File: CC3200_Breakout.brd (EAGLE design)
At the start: 69.8 x 88.9 mm, 101 parts, among them J1 MJ-3536N, J3 SJ-3515-SMT, J4 SJ-3515-SMT, U1 TLV320AIC3254_RHB_32, U15 AT25FS010, U2 TPA2012D2_RTJ_20, Y2 32.768KHz, Y3 407MHz

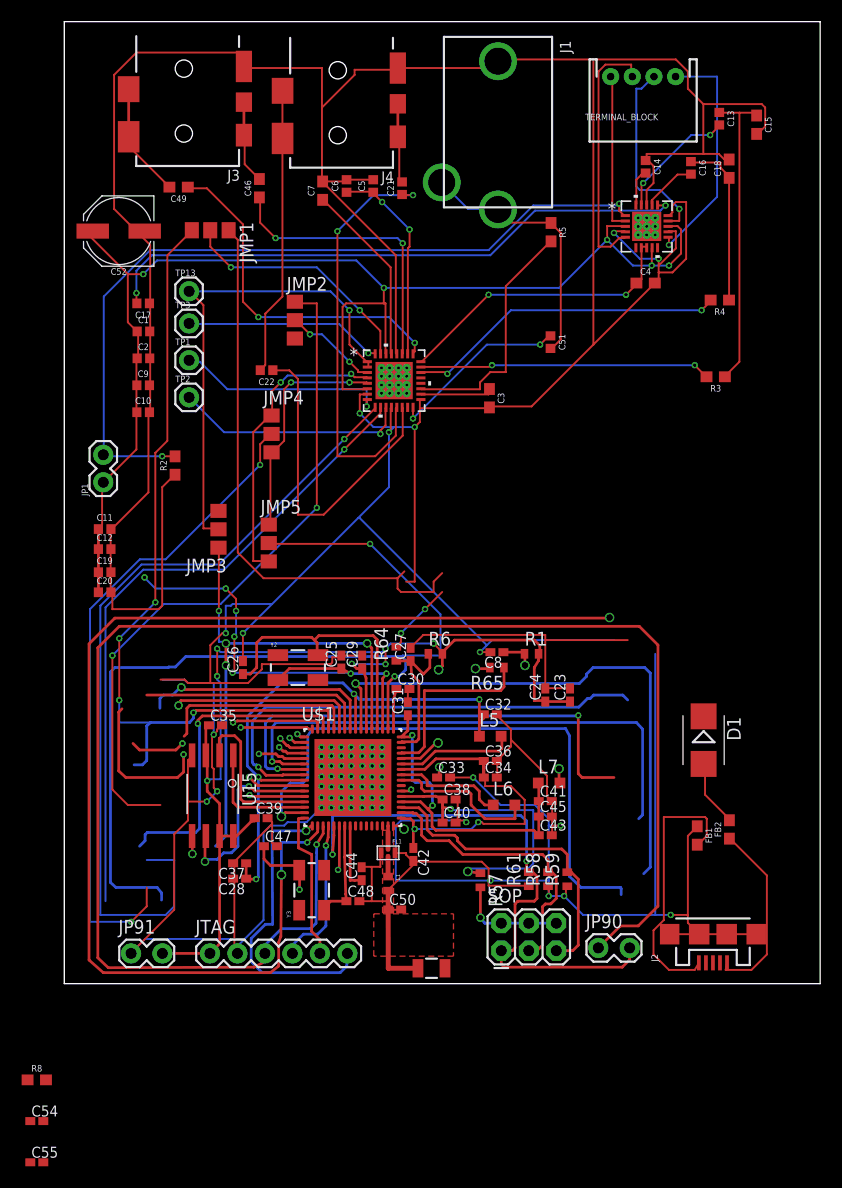
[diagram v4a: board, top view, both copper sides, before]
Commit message: Finished routing and reduced to 2 layers.
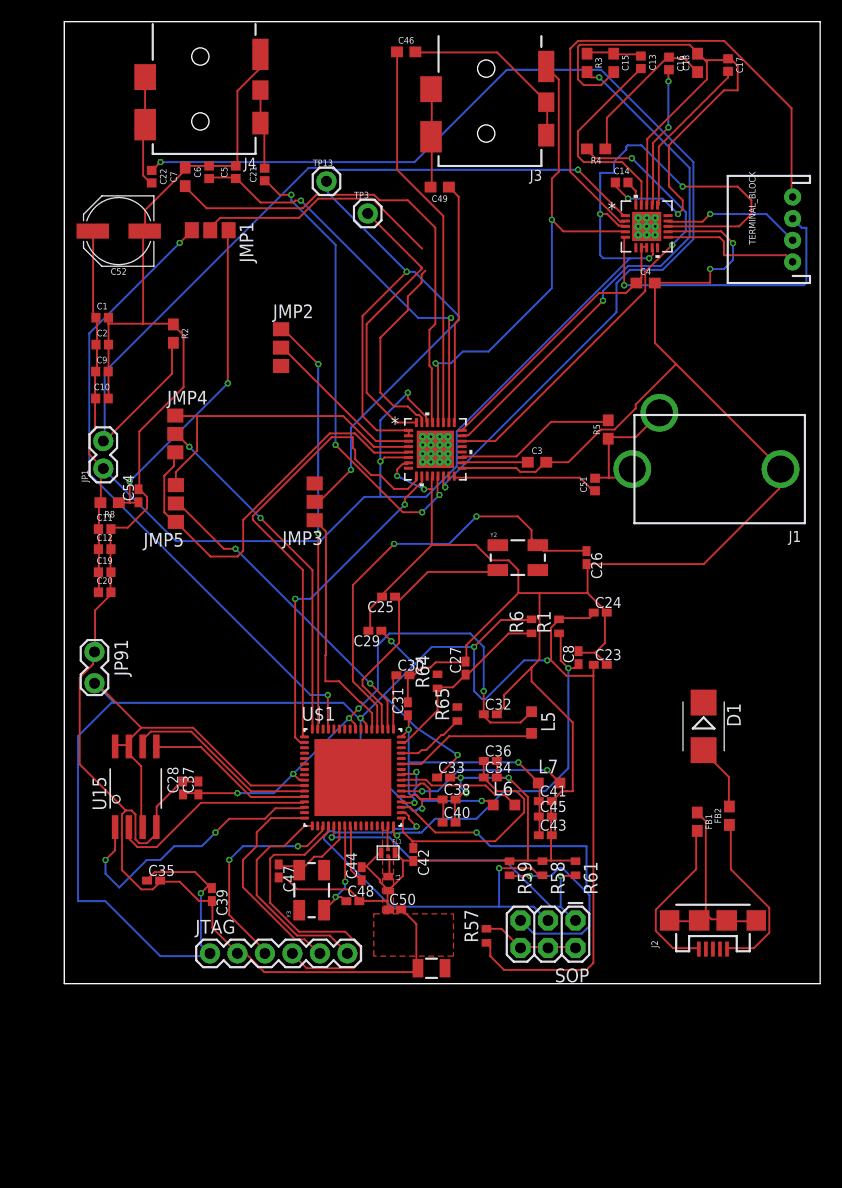
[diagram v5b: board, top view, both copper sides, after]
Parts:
- removed C55: 0.1uF, resistor:C0402K
- removed JP90: M02LOCK, SparkFun-Connectors:1X02_LOCK
- removed TP1, TP2: (no value), SparkFun-Connectors:1X01
- moved C54 58.5 mm to (6.86, 45.1), turned to 90 degrees
- moved C17 58.4 mm to (61.3, 84.9), turned to 270 degrees
- moved R8 53.8 mm to (4.19, 44.5), turned to 180 degrees
- moved J1 45.9 mm to (66.2, 47.5), turned to 90 degrees
- moved C26 33.3 mm to (48.3, 39.4), turned to 270 degrees
- moved R3 31.3 mm to (48.3, 85.1), turned to 270 degrees
- moved J3 27.9 mm to (39.1, 81.6)
- moved JP91 27.9 mm to (2.79, 30.5), turned to 270 degrees
- moved C49 24.1 mm to (34.7, 73.6)
- moved Y2 22.7 mm to (41.9, 39.4)
- moved C22 20.8 mm to (8.08, 74.6), turned to 270 degrees
- moved TERMINAL_BLOCK 19.8 mm to (67.3, 69.7), turned to 90 degrees
- moved TP3 19.4 mm to (28.0, 71.2)
- moved R5 19.0 mm to (50.3, 51.2), turned to 90 degrees
- moved C46 18.5 mm to (31.6, 86.1), turned to 0 degrees
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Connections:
- removed net N$23: TP2.1, U1.11
- removed net N$26: TP1.1, U1.8
- net JTAG_TCK: no longer JP90.1
- net N$22: no longer JP90.2
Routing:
- net GND: track 761.2 -> 538.0 mm, vias 67 -> 11
- net JTAG_TCK: track 145.4 -> 20.2 mm, vias 1 -> 2
- net 18: track 117.1 -> 0.00 mm, vias 3 -> 0
- net V_BATT: track 153.0 -> 233.4 mm, vias 13 -> 7
- net SJ_IN1R: track 30.5 -> 99.9 mm, vias 0 -> 2
- net SDA: track 91.2 -> 30.9 mm
- net SCL: track 104.5 -> 44.3 mm, vias 2 -> 0
- net DOUT_J3: track 86.5 -> 29.8 mm
- net DIN_J3: track 88.4 -> 32.6 mm, vias 3 -> 2
- net 15: track 55.2 -> 0.00 mm, vias 1 -> 0
- net 55: track 51.4 -> 0.00 mm, vias 1 -> 0
- net SPI_MISO: track 49.4 -> 0.00 mm, vias 1 -> 0
- net FSYNC_J3: track 87.0 -> 38.7 mm, vias 3 -> 2
- net SPI_MOSI: track 45.8 -> 0.00 mm, vias 2 -> 0
- net SPI_CS: track 45.1 -> 0.00 mm, vias 1 -> 0
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
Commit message: I get by with a little help from Artur
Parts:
- removed D1: 1A/30V, diode:SMB
- removed FB1, FB2: 40Ω/1.5A, SparkFun-Coils:0603
- removed J2: (no value), SparkFun-Connectors:USB-MICROB
- added C53, C55: 10uF, rcl:C1206
- added IC1: REG1117, burr-brown:SOT223
- added J5: POWER_JACK, SparkFun-Connectors:POWER_JACK_PTH
- added TP1, TP2, TP4: (no value), SparkFun-Connectors:1X01
- moved R57 10.9 mm to (49.9, 3.96), turned to 270 degrees
- moved C47 6.82 mm to (24.6, 5.59), turned to 0 degrees
- moved U$3 3.61 mm to (31.1, 3.71)
- moved C42 2.05 mm to (34.3, 11.7)
- moved C48 0.92 mm to (25.9, 7.11)
- moved Y3 0.51 mm to (22.9, 9.14)
- moved C50 0.51 mm to (30.5, 7.37)
- moved L1 0.51 mm to (29.9, 8.74)
- moved C44 0.44 mm to (27.1, 10.4), turned to 270 degrees
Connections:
- removed net GND: C1.2, C10.2, C11.2, C12.2, C14.1, C15.2, C17.1, C18.2, C19.2, C2.2, C20.2, C23.2, C24.2, C25.2, C26.2, C27.2, C28.2, C29.2, C3.2, C30.2, C31.2, C32.2, C33.2, C34.2, C35.2, C36.2, C37.2, C38.2, C39.2, C4.2, C40.2, C41.2, C42.2, C43.2, C44.2, C45.2, C47.2, C48.2, C5.2, C50.1, C50.2, C52.-, C54.2, C6.2, C7.2, C8.2, C9.2, FB1.1, FL1.2, FL1.4, J1.1, J2.MT1, J2.MT2, J2.P$1, J2.P$2, J3.5, J4.5, JP91.1, JTAG.2, L1.2, R2.1, R58.1, R59.1, R61.1, U$1.EXP, U$3.FEED, U1.12, U1.17, U1.28, U1.33, U1.7, U15.4, U2.12, U2.15, U2.18, U2.21, U2.4
- removed net N$58: D1.A, FB2.2
- removed net N$59: FB2.1, J2.VBUS
- removed net N$60: FB1.2, J2.GND
- removed net VCC_5V_MCU: D1.C
- new net SS: C1.2, C10.2, C11.2, C12.2, C14.1, C15.2, C17.1, C18.2, C19.2, C2.2, C20.2, C23.2, C24.2, C25.2, C26.2, C27.2, C28.2, C29.2, C3.2, C30.2, C31.2, C32.2, C33.2, C34.2, C35.2, C36.2, C37.2, C38.2, C39.2, C4.2, C40.2, C41.2, C42.2, C43.2, C44.2, C45.2, C47.2, C48.2, C5.2, C50.1, C52.-, C53.2, C54.2, C55.2, C6.2, C7.2, C8.2, C9.2, FL1.2, FL1.4, IC1.1, J1.1, J3.5, J4.5, J5.GND, J5.GNDBREAK, JP91.1, JTAG.2, L1.2, R2.1, R58.1, R59.1, R61.1, U$1.EXP, U$3.FEED, U1.12, U1.17, U1.28, U1.33, U1.7, U15.4, U2.12, U2.15, U2.18, U2.21, U2.4
- new net V_IN: C55.1, IC1.3, J5.PWR
- net 58: now also TP1.1
- net 59: now also TP2.1
- net 60: now also TP4.1
- net V_BATT: now also C53.1, IC1.2
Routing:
- net GND: track 538.0 -> 0.00 mm, vias 11 -> 0
- net SS: track 0.00 -> 296.9 mm, vias 0 -> 10
- net N$10: track 22.1 -> 44.4 mm, vias 0 -> 2
- net 59: track 0.00 -> 21.3 mm, vias 0 -> 1
- net 58: track 0.00 -> 21.0 mm, vias 0 -> 1
- net N$21: track 43.1 -> 24.4 mm, vias 2 -> 1
- net N$59: track 16.1 -> 0.00 mm
- net N$60: track 15.5 -> 0.00 mm
- net V_IN: track 0.00 -> 13.8 mm
- net CODEC_RESET: track 60.1 -> 73.4 mm
- net 60: track 0.00 -> 10.1 mm, vias 0 -> 1
- net V_BATT: track 233.4 -> 224.9 mm, vias 7 -> 10
- net N$17: track 51.0 -> 57.5 mm
- net N$58: track 6.18 -> 0.00 mm
- net BCLK_J3: track 22.3 -> 27.9 mm
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- added copper zone on layer 1, net SS
- added copper zone on layer 16, net SS
- removed copper zone on layer 1, net N$16
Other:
- board text added: "& TA"
- board text added: "Team 10"
